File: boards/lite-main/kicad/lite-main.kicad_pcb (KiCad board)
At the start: 2 copper layers, 100 x 90 mm, 138 parts, among them J1 USB4105-GF-A-120, J2 RCA line in, J3 RCA sub out, J4 DB128V-5.08-4P, Q1 AO4485, Q2 MMBT3904, Q3 MMBT3904, Q4 MMBT3904, SW1 TS-1187A, SW2 TS-1187A, SW3 TS-1187A, U1 CH224A, U2 TPS54302, U3 SY8089A1AAC, U4 LP5907-3.3, U5 ESP32-WROVER-E-N8R8, U6 CH340C, U7 ES8388, U8 TPA3118D2, U9 IRM-3638T

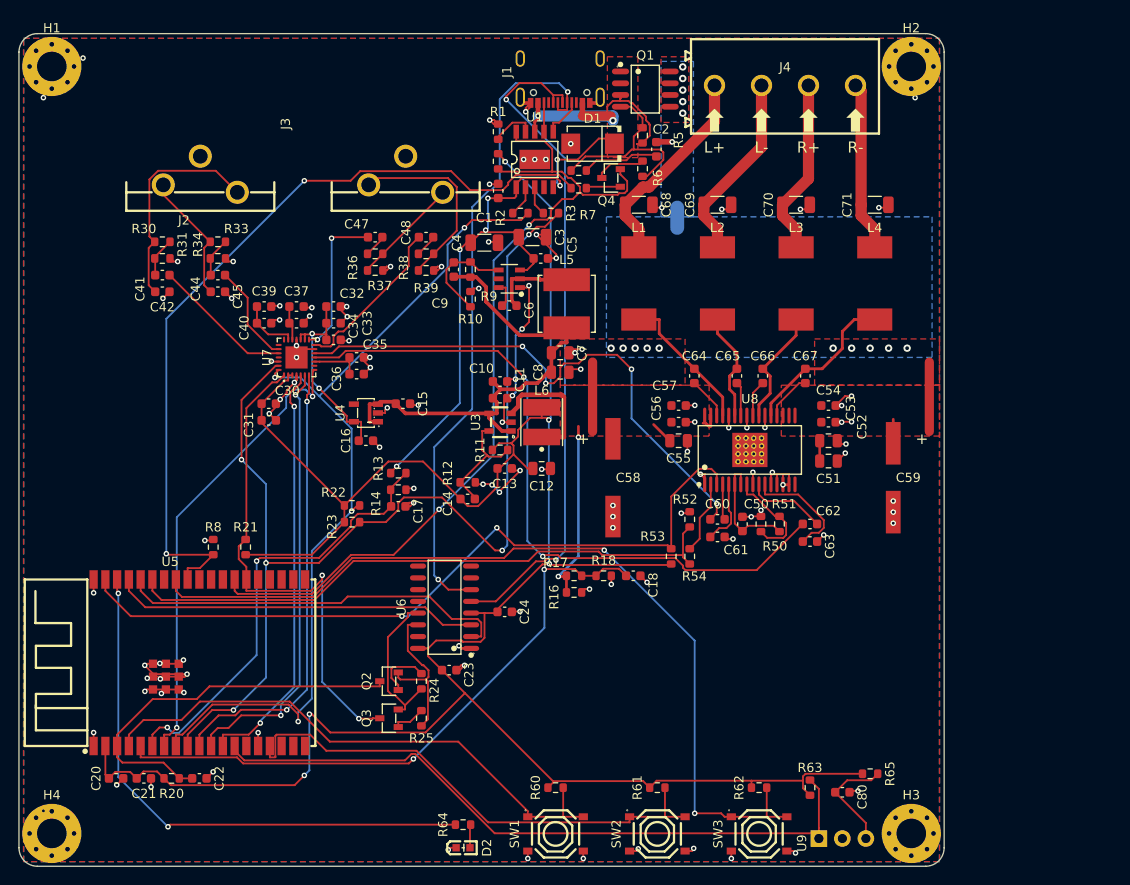
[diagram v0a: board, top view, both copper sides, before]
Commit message: The hifi boards' +3V3 is budgeted, and built, for the ESP32 module's 500 mA radio peaks
* The hifi boards' +3V3 is budgeted and built for the ESP32 module's 50…

…0 mA radio peaks

core: +3V3 budget 0.3 -> 0.8 A (the module's 500 mA plus everything else on
the rail); the In2 plane gives 2.4 mV at the module (check_irdrop), SY8089
2 A and its inductor carry it.
lite-main: +3V3 budget 0.35 -> 0.55 A at dT 20 C (as the board's other
rails), vias rated 1 A like VBUS's; the 95 mm track path from L6 to the
module widened from 0.2 mm (0.3 mm where clearance allows, 0.204-0.25 mm
elsewhere), second vias at three of four layer changes, via hwde route_edit;
IR drop at the peak 114 -> 85 mV. Gerbers regenerated. hwde check_fw,
check_current, check_pdn pass on both boards.

* lite-main +3V3: snap the nudged joints back onto the 45-degree grid (…

…route_cleanup --snap-only, one joint slid along its diagonal); Gerbers regenerated
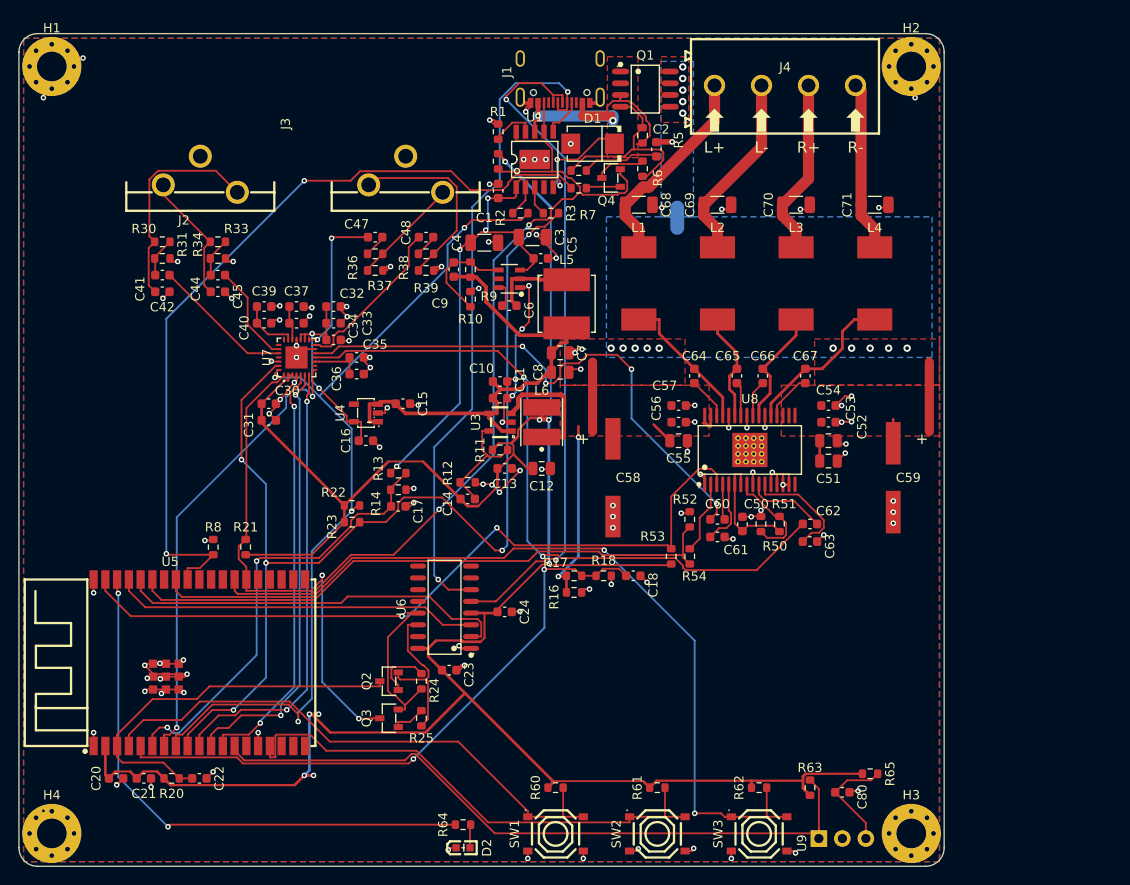
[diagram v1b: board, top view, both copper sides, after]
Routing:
- net +3V3: track 264.9 -> 271.1 mm, vias 5 -> 8

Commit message: The boards will work on the first spin: independent engineering reviews of Lite and core, fixes and contingencies built…
* First-spin review: the brief each domain reviewer works from

* First-spin review: partial drafts saved before the reviewers' login d…

…ropped

* First-spin review: power, audio, digital and thermal reviews of lite-…

…main and core, with their sims

* core carries its EasyEDA CPL model cache, so its dfm gate runs withou…

…t EasyEDA (red on 403 otherwise); DFM review

* First-spin review: parts pin-to-pad audit of both boards

* Lite board after the first-spin review: amp SDZ, PVDD switch hold-off…

… and soft start, line-in headroom, 5 V loop, RCA slots, HRO USB-C and CH340B, speaker loopback taps; regenerated on hwde c23e27e, all gates pass

Review-2 findings fixed on lite-main as an ECO on the routed board (no
re-route): AUDIO-4/DIGITAL-14, POWER-3/4/10, AUDIO-7, DFM-2, stock swaps.
Also: the speaker loopback taps (task 261029-033806) and the hwde refresh
(task 261029-004401) for this board. Known-unknowns list and its order-step
check (tools/known_unknowns.py). Unit cost at 100: 13.16 (was 13.05).

* core (Plus/Ultra) after the first-spin review: TCA9539 with ESP32 res…

…et, 5 A path via patches and through-hole USB4085, antenna keep-out, PVDD switch SOA and PD-PG gating, OPA1678 headroom, RCA and TOSLINK holes, front IR, 49.152 MHz DAC clock, speaker loopback taps; all gates pass

Review-2 blockers fixed on core: DIGITAL-1/2/PARTS-4, POWER-1, DFM-1, PARTS-7;
THERMAL-1 handled by a lid-pressed heatsink plus firmware governor (no room
for clip holes). Majors: POWER-2/6, AUDIO-1/2/3, DIGITAL-19, DFM-4. Done as an
ECO on the routed board; Ultra zone-B taps left out (no control line).

* First-spin review: every finding's disposition, known-unknowns resolv…

…ed for Lite and Plus (order gate by tier), firmware duties for core, R45 2.2k, honest TPA3221 thermal constraint, Plus/Ultra cost estimate

* Heatsink options for the TPA3221 checked aga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
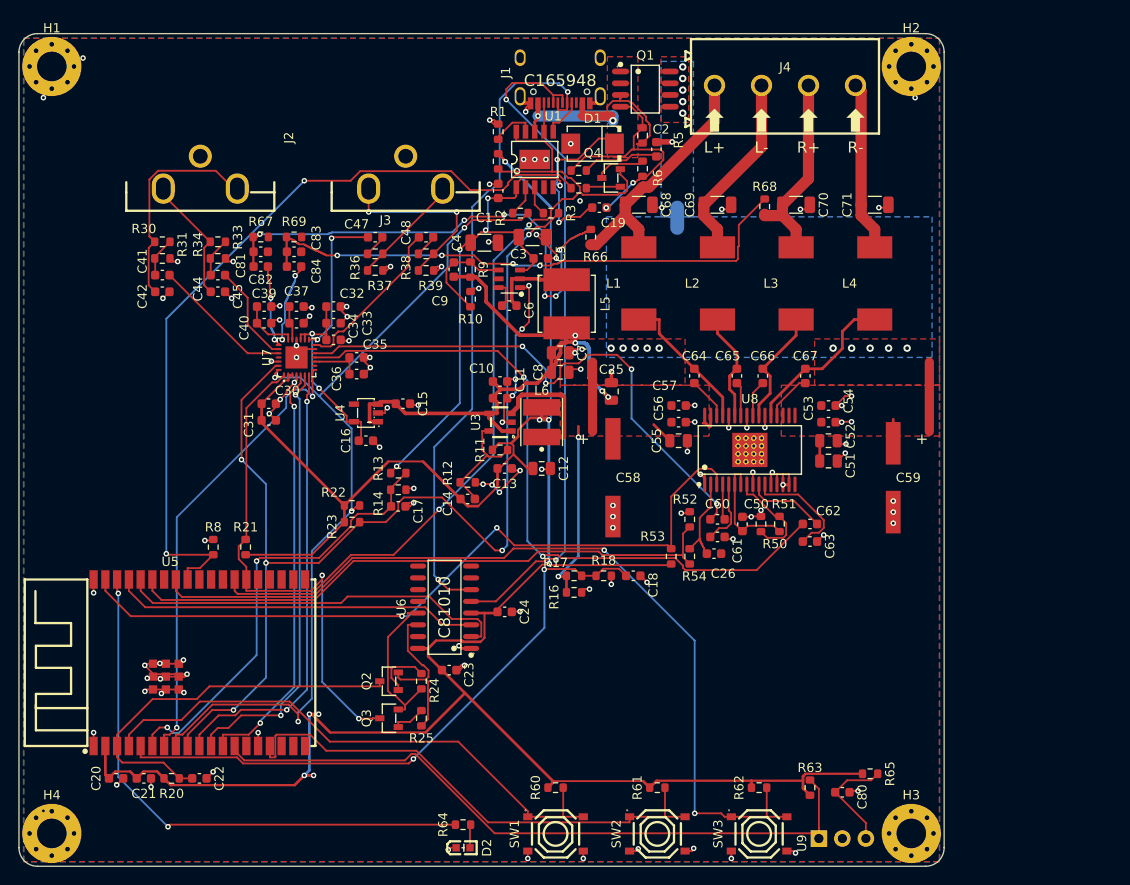
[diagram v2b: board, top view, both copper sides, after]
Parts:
- added C19: 4.7uF, Capacitor_SMD:C_0603_1608Metric, F.Cu at (85.6, 79.1)
- added C25: 22uF, Capacitor_SMD:C_0805_2012Metric, F.Cu at (86.9, 99.0)
- added C26: 47nF, Capacitor_SMD:C_0603_1608Metric, F.Cu at (98.0, 116.5)
- added C81: 470pF, Capacitor_SMD:C_0603_1608Metric, F.Cu at (49.0, 83.9)
- added C82: 1uF, Capacitor_SMD:C_0603_1608Metric, F.Cu at (49.0, 85.5)
- added C83: 470pF, Capacitor_SMD:C_0603_1608Metric, F.Cu at (52.6, 83.9)
- added C84: 1uF, Capacitor_SMD:C_0603_1608Metric, F.Cu at (52.6, 85.5)
- added R66: 100k, Resistor_SMD:R_0603_1608Metric, F.Cu at (84.7, 82.3)
- added R67: 10k, Resistor_SMD:R_0603_1608Metric, F.Cu at (49.0, 82.3)
- added R68: 100k, Resistor_SMD:R_0603_1608Metric, F.Cu at (103.5, 79.0)
- added R69: 10k, Resistor_SMD:R_0603_1608Metric, F.Cu at (52.6, 82.3)
- C9: value 100pF -> 47pF
- J1: value USB4105-GF-A-120 -> TYPE-C-31-M-12; footprint aiee:USB-C-SMD_MC-311D -> aiee:USB-C_SMD-TYPE-C-31-M-12_1
- R30, R33: value 10k -> 15k
- R54: value 100k -> 10k
- R6: value 47k -> 220k
- U6: value CH340C -> CH340B
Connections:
- U7 pad 21: unconnected-(U7-RIN2-Pad21) -> /TAP_R_C
- U7 pad 22: unconnected-(U7-LIN2-Pad22) -> /TAP_L_C
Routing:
- net /TAP_R: track 0.00 -> 61.2 mm, vias 0 -> 4
- net /TAP_L: track 0.00 -> 54.2 mm, vias 0 -> 6
- net +5V: track 52.8 -> 68.9 mm, vias 0 -> 4
- net /TAP_L_C: track 0.00 -> 8.99 mm, vias 0 -> 2
- net /TAP_R_C: track 0.00 -> 8.98 mm, vias 0 -> 2
- net VBUS: track 91.7 -> 100.5 mm, vias 8 -> 9
- net /PSW_G: track 21.5 -> 27.3 mm, vias 0 -> 2
- net /SPK_L_P: track 22.5 -> 27.5 mm
- net /SPK_R_P: track 19.3 -> 21.3 mm
- net /AMP_SDZ: track 7.90 -> 9.85 mm
- net /USB_DM: track 71.4 -> 73.0 mm
- net GND: track 162.1 -> 163.3 mm, vias 115 -> 117
- net /USB_DP: track 73.1 -> 73.9 mm
- net /SUB_R: track 21.0 -> 21.1 mm, vias 0 -> 2

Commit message: Lite's VBUS TVS D1 holds the 21 V PD rail: SMBJ22A (22 V standoff) in place of SMBJ20A, fab and order files regenerated
D1 BORN SMBJ22A C151920, same SMB footprint and pin 1 = K as the MDD SMBJ20A C364296.
Fab BOM/CPL/prebuy and the Digi-Key/Mouser BOMs (stale since the 10-29 ECO) rebuilt
under today's hwde; dfm gate PASS. Ledger: D1 rating verified from BORN's table.
Known unknowns: power:10, thermal:30, parts:45 updated; --check --tier lite 0 open.
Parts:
- D1: value SMBJ20A -> SMBJ22A
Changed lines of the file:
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@@
 			)
 		)
-		(property "Value" "SMBJ20A"
+		(property "Value" "SMBJ22A"
 			(at 0 4 180)
 			(layer "F.Fab")
@@
 			)
 		)
-		(property "LCSC Part" "C364296"
+		(property "LCSC Part" "C151920"
 			(at 0 0 180)
 			(layer "F.Fab")
@@
 			)
 		)
-		(property "LCSC" "C364296"
+		(property "LCSC" "C151920"
 			(at 0 0 180)
 			(layer "F.SilkS")

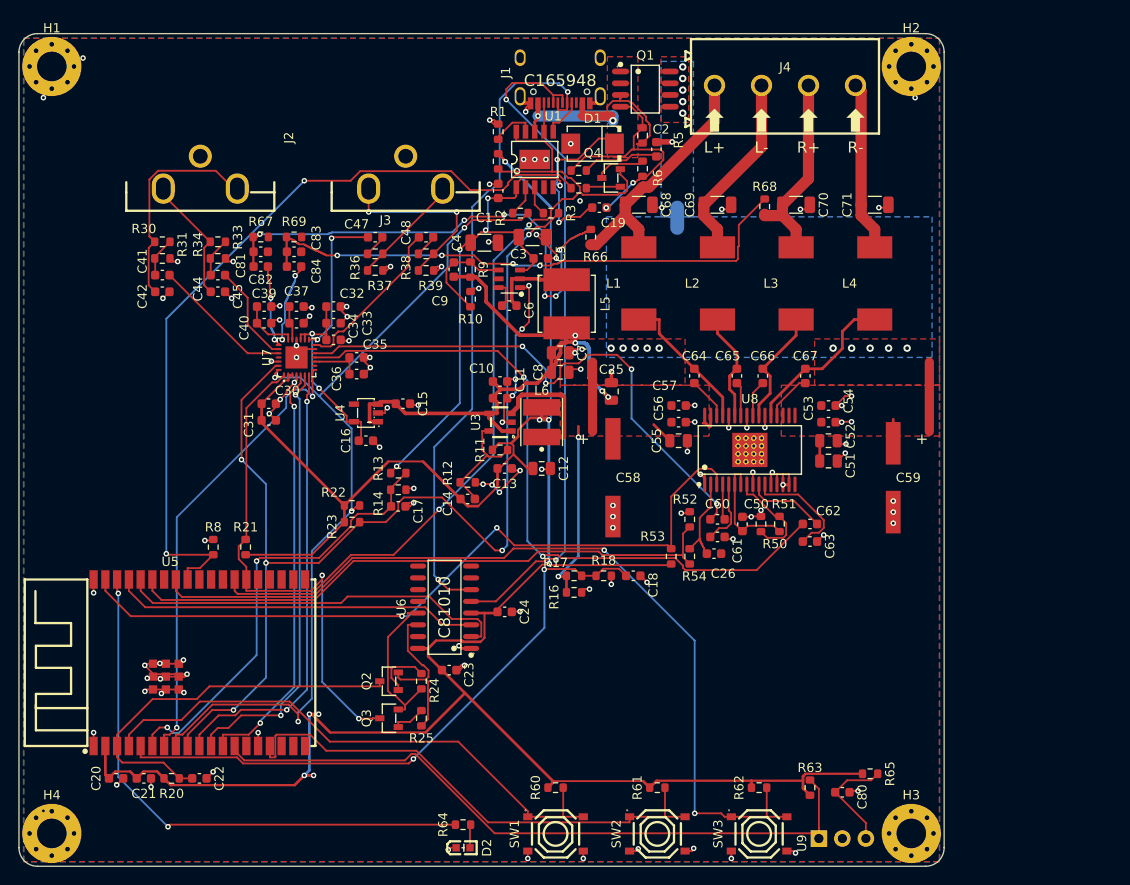
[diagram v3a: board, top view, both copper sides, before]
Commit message: Lite's speaker outputs are four board-mounted 4 mm banana sockets (Amass 24.243, JLC-fitted): J4-J7 on a 118 mm wide board, L1-L4 2.2 mm toward U8, caps and taps re-placed, speaker copper re-routed
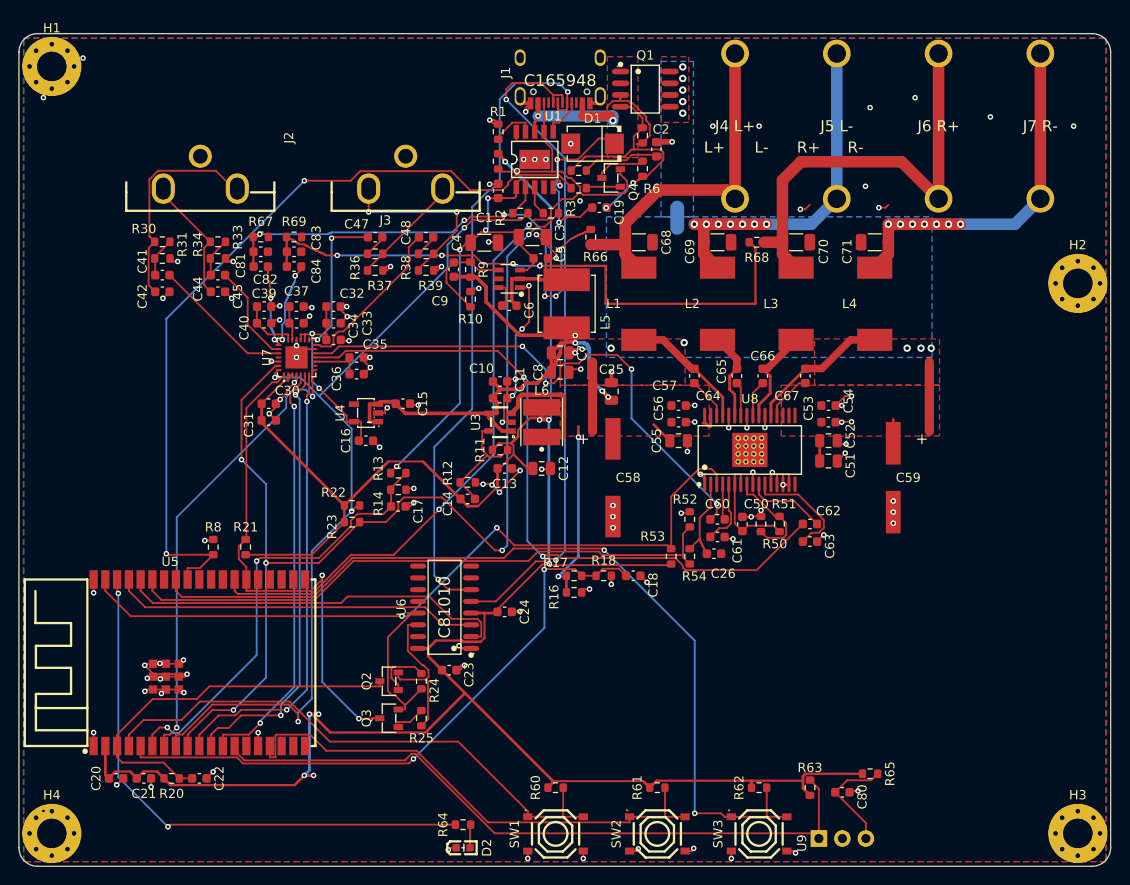
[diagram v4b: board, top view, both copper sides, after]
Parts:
- added J5: 24.243 black, aiee:CONN-TH_24.243.2, F.Cu at (111.3, 70.3)
- added J6: 24.243 red, aiee:CONN-TH_24.243.1_RED, F.Cu at (122.3, 70.3)
- added J7: 24.243 black, aiee:CONN-TH_24.243.2, F.Cu at (133.3, 70.3)
- J4: value DB128V-5.08-4P -> 24.243 red; footprint aiee:CONN-TH_4P-P5.08_DIBO_DB128V-5.08 -> aiee:CONN-TH_24.243.1_RED
- moved H2 29.6 mm to (137.3, 87.3)
- moved H3 18.0 mm to (137.3, 146.8)
- moved J4 6.97 mm to (100.3, 70.3), turned to 90 degrees
- moved C68 4.05 mm to (89.9, 82.9)
- moved C69 4.05 mm to (98.4, 82.9)
- moved C70 4.05 mm to (106.9, 82.9)
- moved C71 4.05 mm to (115.4, 82.9), turned to 180 degrees
- moved R68 3.95 mm to (102.6, 82.9), turned to 180 degrees
- moved L1 2.20 mm to (89.9, 89.5)
- moved L2 2.20 mm to (98.4, 89.5)
- moved L3 2.20 mm to (106.9, 89.5)
- moved L4 2.20 mm to (115.4, 89.5)
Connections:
- net /IR_VCC renamed IR_VCC
- J4 pad 2: /SPK_L_N -> /SPK_L_P
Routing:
- net /SPK_R_N: track 18.4 -> 46.4 mm, vias 0 -> 7
- net /SPK_R_P: track 21.3 -> 47.1 mm
- net /SPK_L_N: track 20.7 -> 45.4 mm, vias 0 -> 7
- net /SPK_L_P: track 27.5 -> 38.6 mm
- net /TAP_R: track 61.2 -> 66.2 mm
- net GND: track 163.3 -> 160.9 mm, vias 117 -> 121
- net /OUT_L_N: track 11.8 -> 9.59 mm
- net /OUT_R_N: track 17.4 -> 15.4 mm
- net /OUT_R_P: track 12.7 -> 10.8 mm
- net /OUT_L_P: track 15.4 -> 13.6 mm
- net PVDD: vias 18 -> 13
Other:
- board size 100 x 90 mm -> 118 x 90 mm
- board text added: "J4 L+"
- board text added: "J5 L-"
- board text added: "J6 R+"
- board text added: "J7 R-"

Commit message: Lite and core converge: review rounds against app notes, reference designs and known field issues until a round finds n…
* Review round 2: the brief each reviewer works from (app notes, refere…

…nce designs, field issues)

* Review round 2: partial drafts (power, amp, audio, system, layout) an…

…d their tests, saved before the session dropped

* Review round 2: amp review (2 majors on core: bootstrap and PVDD HF c…

…ap placement) and its tests

* Review round 2: audio-chain review (3 majors: core VREF filtering, Li…

…te sub-out power-loss thump, core DJ-direct subs silent) and its sims

* Review round 2: power review (4 majors: core PVDD turn-on SOA regress…

…ion, charger peak current under the average governor, core VBUS unknown, EPR step) and its benches

* Review round 2: digital review (3 majors: core GPIO0 strap on interna…

…l resets, LAN8720 PHY address, Ultra front board undriven) and its tests

* Review round 2: system/field review (4 majors: governor and clipping,…

… Lite L1 thermal, core GPIO0 on restart, DJ-direct thermal on core) and its tests

* Firmware after review round 2: the governor limits on the unclipped p…

…rogram and each block's peak, Lite's L1 thermal limit, core reads the charger's PDOs and waits for EPR, 500 ms PVDD soft start, PHY clock off before a restart, OTW step-down, amps held across an input change and until the codec settles, input kept in NVS

R3-SYSTEM-1/2/3/5, R3-POWER-2(firmware half)/3/4/5, R3-DIGITAL-1(firmware half); round-1 duties L1 L4 C1 C2 C5. Host tests pass (make in firmware/test).

* Merge branch 'main' of /hive/run/main.bundle into hive/w-261030-15165…

…6-0a0fabd0ce

* Review round 2: layout/DFM/thermal review (blocker: core J4/J5 RCA fo…

…otprints never took round 1's leg holes; major: core amp input routing) and its tests

* Lite's sub outs mute on power loss (review-3 R3-AUDIO-2): a +5V sense…

… holds two back-to-back 2N7002s off; when +5V drops they short SUB_L/SUB_R to GND from a 22 uF reservoir for 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
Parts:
- added C90: 22uF, Capacitor_SMD:C_0805_2012Metric, F.Cu at (72.6, 93.0)
- added Q11: MMBT3904, aiee:SOT-23-3_L2.9-W1.3-P1.90-LS2.4-BR, F.Cu at (68.9, 92.1)
- added Q12: MMBT3904, aiee:SOT-23-3_L2.9-W1.3-P1.90-LS2.4-BR, F.Cu at (65.3, 92.1)
- added Q13: 2N7002, aiee:SOT-23-3_L2.9-W1.3-P1.90-LS2.4-BR, F.Cu at (63.9, 89.0)
- added Q14: 2N7002, aiee:SOT-23-3_L2.9-W1.3-P1.90-LS2.4-BR, F.Cu at (61.8, 92.1)
- added Q15: 2N7002, aiee:SOT-23-3_L2.9-W1.3-P1.90-LS2.4-BR, F.Cu at (67.5, 89.0)
- added R80: 120k, Resistor_SMD:R_0603_1608Metric, F.Cu at (73.5, 91.2)
- added R81: 22k, Resistor_SMD:R_0603_1608Metric, F.Cu at (56.4, 87.9)
- added R82: 47k, Resistor_SMD:R_0603_1608Metric, F.Cu at (59.4, 87.9)
- R36, R38: value 100R -> 1k
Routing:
- net /MUTE_DET: track 0.00 -> 28.2 mm, vias 0 -> 4
- net /MUTE_RES: track 0.00 -> 21.1 mm, vias 0 -> 2
- net +5V: track 68.9 -> 87.2 mm, vias 4 -> 6
- net /SUB_MUTE: track 0.00 -> 14.2 mm, vias 0 -> 2
- net /MUTE_S: track 0.00 -> 7.52 mm, vias 0 -> 2
- net /SUB_R: track 21.1 -> 27.3 mm
- net /SUB_L: track 11.8 -> 15.9 mm, vias 0 -> 2
- net GND: vias 121 -> 123
